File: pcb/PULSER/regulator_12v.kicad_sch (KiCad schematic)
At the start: 5 parts, among them U5 LMV7219M5

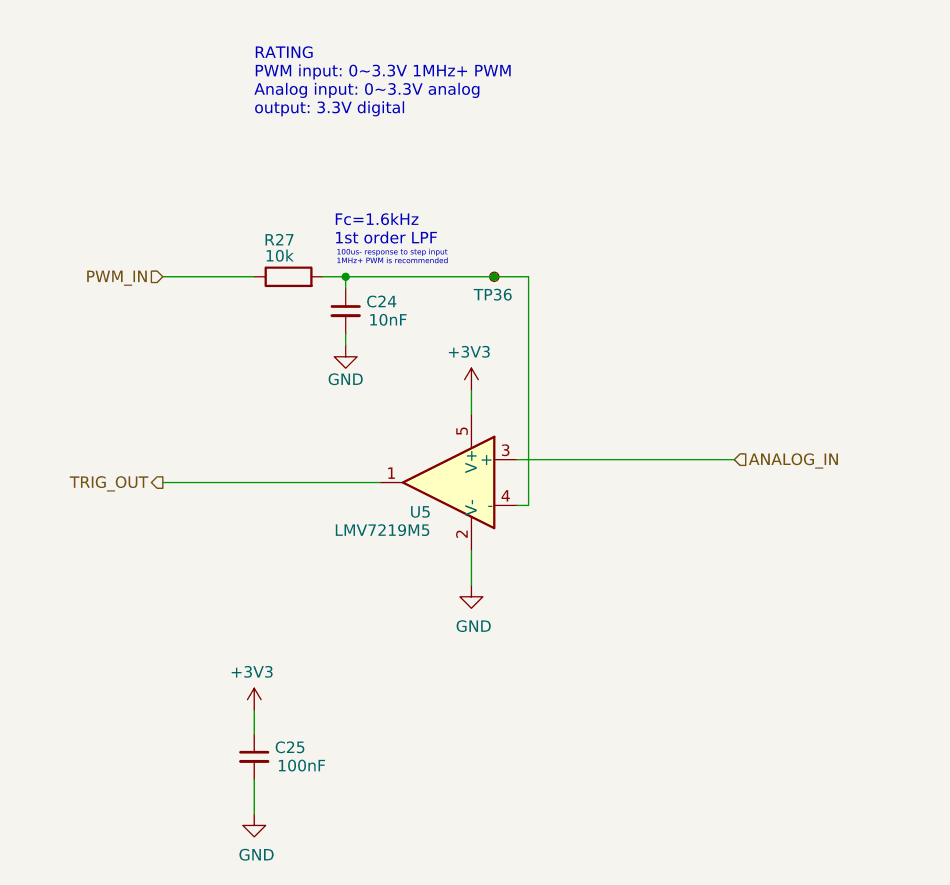
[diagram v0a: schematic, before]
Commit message: Rename pcb & firmware to be more meaningful
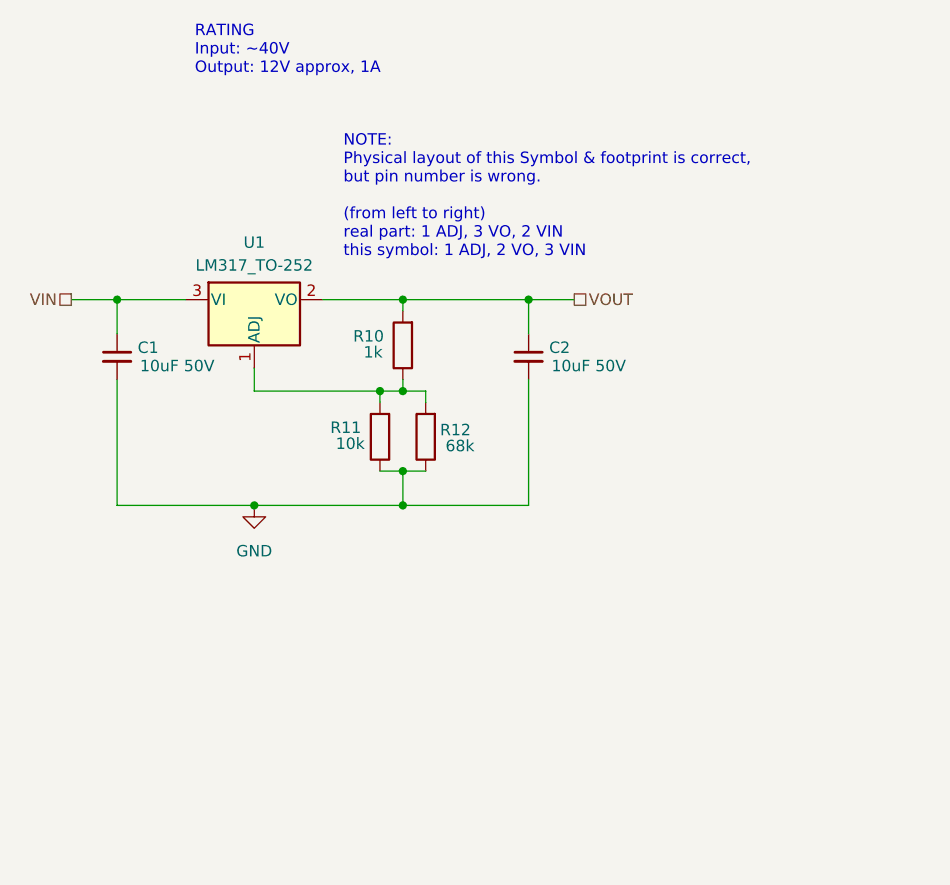
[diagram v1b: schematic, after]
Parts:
- removed C24: 10nF, Capacitor_SMD:C_0603_1608Metric, symbol Device:C_Small
- removed C25: 100nF, Capacitor_SMD:C_0603_1608Metric, symbol Device:C_Small
- removed R27: 10k, Resistor_SMD:R_0603_1608Metric, symbol Device:R
- removed TP36: TestPoint, TestPoint:TestPoint_Pad_D1.5mm, symbol Connector:TestPoint_Small
- removed U5: LMV7219M5, Package_TO_SOT_SMD:SOT-23-5, symbol Comparator:LMV7219M5
- added C1, C2: 10uF 50V, Capacitor_SMD:C_1206_3216Metric, symbol Device:C_Small
- added R10: 1k, Resistor_SMD:R_0603_1608Metric, symbol Device:R
- added R11: 10k, Resistor_SMD:R_0603_1608Metric, symbol Device:R
- added R12: 68k, Resistor_SMD:R_0603_1608Metric, symbol Device:R
- added U1: LM317_TO-252, Package_TO_SOT_SMD:TO-252-2, symbol Regulator_Linear:LM317_TO-252
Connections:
- net GND: now also C1.2, C2.2, R11.1, R12.1
- new net: R10.1, R11.2, R12.2, U1.1 (ADJ)
- new net VIN: C1.1, U1.3 (VI)
- new net VOUT: C2.1, R10.2, U1.2 (VO)
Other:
- note added: "NOTE: Physical layout of this Symbol & footprint is correct, but pin number is wrong. (from left to right) real part: 1 ADJ, 3 VO, 2 VIN this symbol: 1 ADJ, 2 VO, 3 VIN"
- note added: "RATING Input: ~40V Output: 12V approx, 1A"
- note removed: "100us- response to step input 1MHz+ PWM is recommended"
- note removed: "Fc=1.6kHz 1st order LPF"
- note removed: "RATING PWM input: 0~3.3V 1MHz+ PWM Analog input: 0~3.3V analog output: 3.3V digital"

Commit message: PULSER r2 pulse shaper draft
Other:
- title: CTRL-MINI-ED -> PULSER
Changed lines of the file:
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@@
 (kicad_sch
-	(version 20231120)
+	(version 20250114)
 	(generator "eeschema")
-	(generator_version "8.0")
+	(generator_version "9.0")
 	(paper "A4")
 	(title_block
-		(title "CTRL-MINI-ED")
-		(date "2024-12-11")
-		(rev "1")
+		(title "PULSER")
+		(date "2025-02-14")
+		(rev "2")
 		(company "Spark Project")
 		(comment 1 "Author: 夕月霞 (xyx)")
 		(comment 2 "EDM Pulse Generator Board")
+	)
+	(text "NOTE:\nPhysical layout of this Symbol & footprint is correct,\nbut pin number is wrong.\n\n(from left to right)\nreal part: 1 ADJ, 3 VO, 2 VIN\nthis symbol: 1 ADJ, 2 VO, 3 VIN\n"
+		(exclude_from_sim no)
+		(at 81.026 39.37 0)
+		(effects
+			(font
+				(size 1.27 1.27)
+			)
+			(justify left)
+		)
+	)
+	(text "RATING\nInput: ~40V\nOutput: 12V approx, 1A\n"
+		(exclude_from_sim no)
+		(at 64.516 23.114 0)
+		(effects
+			(font
+				(size 1.27 1.27)
+			)
+			(justify left)
+		)
 	)
 	(junction
@@
 			"4ZK0ekyCWdiZWsxzXcAo9v1YUwMLO1OLPV0XsB1b2ZmqWdiZqkjfmi5gpus6tjNTbillXRdhmoOF"
 			"namOFyRzFTVkDylMdSzsTHVSCb1lTF47jEkoCztTraSGSlLrMgljYWeqk9wVVFLrMgljYWeqNc91"
-			"AeOY57oA0xws7Ey1krqCSmpdJmEs7Ey1khoqSa3LJMz/BzS5D5EH5SGfAAAAAElFTkSuQmCC"
-		)
-	)
-	(text "NOTE:\nPhysical layout of this Symbol & footprint is correct,\nbut pin number is wrong.\n\n(from left to right)\nreal part: 1 ADJ, 3 VO, 2 VIN\nthis symbol: 1 ADJ, 2 VO, 3 VIN\n"
-		(exclude_from_sim no)
-		(at 81.026 39.37 0)
+			"AeOY57oA0xws7Ey1krqCSmpdJmEs7Ey1khoqSa3LJMz/BzS5D5EH5SGfAAAAAElFTkSuQmCCAAAA"
+			"AAAAAAAAAAAAAAAAAAAAAAAAAAAAAAAAAAAAAAAAAAAAAAAAAAAAAAAAAAAAAAAAAAAAAAAAAAAA"
+			"AAAAAAAAAAAAAAAAAAAAAAAAAAAAAAAAAAAAAAAAAAAAAAAAAAAAAAAAAAAAAAAAAAAAAAAAAAAA"
+			"AAAAAAAAAAAAAAAAAAAAAAAAAAAAAAAAAAAAAAAAAAAAAAAAAAAAAAAAAAAAAAAAAAAAAAAAAAAA"
+			"AAAAAAAAAAAAAAAAAAAAAAAAAAAAAAAAAAAAAAAAAAAAAAAAAAAAAAAAAAAAAAAAAAAAAAAAAAAA"
+			"AAAAAAAAAAAAAAAAAAAAAAAAAAAAAAAAAAAAAAAAAAAAAAAAAAAAAAAAAAAAAAAAAAAAAAAAAAAA"
+			"AAAAAAAAAAAAAAAAAAAAAAAAAAAAAAAAAAAAAAAAAAAAAAAAAAAAAAAAAAAAAAAAAAAAAAAAAAAA"
+			"AAAAAAAAAAAAAAAAAAAAAAAAAAAAAAAAAAAAAAAAAAAAAAAAAAAAAAAAAAAAAAAAAAAAAAAAAAAA"
+			"AAAAAAAAAAAAAAAAAAAAAAAAAAAAAAAAAAAAAAAAAAAAAAAAAAAAAAAAAAAAAAAAAAAAAAAAAAAA"
+			"AAAAAAAAAAAAAAAAAAAAAAAAAAAAAAAAAAAAAAAAAAAAAAAAAAAAAAAAAAAAAAAAAAAAAAAAAAAA"
+			"AAAAAAAAAAAAAAAAAAAAAAAAAAAAAAAAAAAAAAAAAAAAAAAAAAAAAAAAAAAAAAAAAAAAAAAAAAAA"
+			"AAAAAAAAAAAAAAAAAAAAAAAAAAAAAAAAAAAAAAAAAAAAAAAAAAAAAAAAAAAAAAAAAAAAAAAAAAAA"
+			"AAAAAAAAAAAAAAAAAAAAAAAAAAAAAAAAAAAAAAAAAAAAAAAAAAAAAAAAAAAAAAAAAAAAAAAAAAAA"
+			"AAAAAAAAAAAAAAAAAAAAAAAAAAAAAAAAAAAAAAAAAAAAAAAAAAAAAAAAAAAAAAAAAAAAAAAAAAAA"
+			"AAAAAAAAAAAAAAAAAAAAAAAAAAAAAAAAAAAAAAAAAAAAAAAAAAAAAAAAAAAAAAAAAAAAAAAAAAAA"
+			"AAAAAAAAAAAAAAAAAAAAAAAAAAAAAAAAAAAAAAAAAAAAAAAAAAAAAAAAAAAAAAAAAAAAAAAAAAAA"
+			"AAAAAAAAAAAAAAAAAAAAAAAAAAAAAAAAAAAAAAAAAAAAAAAAAAAAAAAAAAAAAAAAAAAAAAAAAAAA"
+			"AAAAAAAAAAAAAAAAAAAAAAAAAAAAAAAAAAAAAAAAAAAAAAAAAAAAAAAAAAAAAAAAAAAAAAAAAAAA"
+			"AAAAAAAAAAAAAAAAAAAAAAAAAAAAAAAAAAAAAAAAAAAAAAAAAAAAAAAAAAAAAAAAAAAAAA=="
+		)
+	)
+	(hierarchical_label "VIN"
+		(shape passive)
+		(at 50.8 50.8 180)
 		(effects
 			(font
 				(size 1.27 1.27)
 			)
-			(justify left)
-		)
-	)
-	(text "RATING\nInput: ~40V\nOutput: 12V approx, 1A\n"
-		(exclude_from_sim no)
-		(at 64.516 23.114 0)
-		(effects
-			(font
-				(size 1.27 1.27)
-			)
-			(justify left)
-		)
-	)
-	(hierarchical_label "VIN"
-		(shape passive)
-		(at 50.8 50.8 180)
-		(fields_autoplaced yes)
-		(effects
-			(font
-				(size 1.27 1.27)
-			)
 			(justify right)
 		)
@@
 		(shape passive)
 		(at 106.68 50.8 0)
-		(fields_autoplaced yes)
 		(effects
 			(font
@@
 		(at 71.12 73.66 0)
 		(unit 1)
-		(exclude_from_sim yes)
+		(exclude_from_sim no)
 		(in_bom yes)
 		(on_board yes)
